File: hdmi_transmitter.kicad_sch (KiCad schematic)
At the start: 42 parts, among them J10 Conn_01x03, J2 47151-0001, U2 LT1963AxST-1.8, U3 TPD12S520DBT

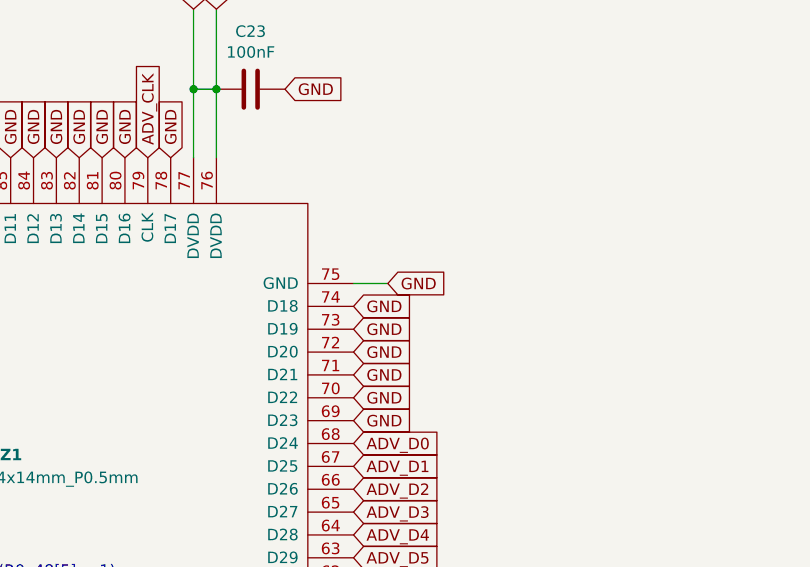
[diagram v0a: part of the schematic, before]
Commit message: Prod version of OpenAARS 5.0 design.
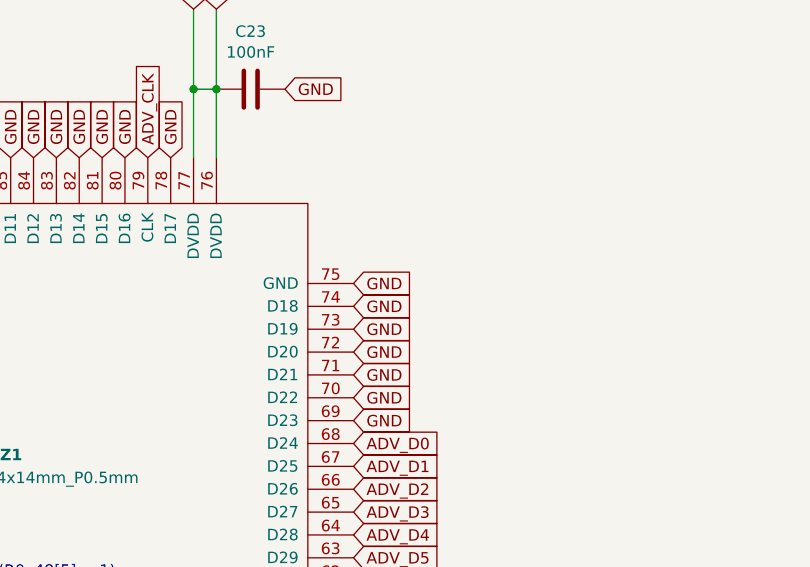
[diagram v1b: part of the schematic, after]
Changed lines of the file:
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@@
-    (stroke (width 0) (type default))
-  )
-  (wire (pts (xy 247.015 75.565) (xy 250.825 75.565))
     (stroke (width 0) (type default))
   )
@@
     )
   )
-  (global_label "GND" (shape input) (at 250.825 75.565 0) (fields_autoplaced)
-    (effects (font (size 1.27 1.27)) (justify left))
-    (property "Intersheetrefs" "${INTERSHEET_REFS}" (at 0 0 0)
-      (effects (font (size 1.27 1.27)) hide)
-    )
+  (global_label "GND" (shape input) (at 247.015 75.565 0) (fields_autoplaced)
+    (effects (font (size 1.27 1.27)) (justify left))
+    (property "Intersheetrefs" "${INTERSHEET_REFS}" (at -3.81 0 0)
+      (effects (font (size 1.27 1.27)) hide)
+    )
